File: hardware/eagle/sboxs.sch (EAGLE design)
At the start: 32 parts, among them U1 TXS0101_DBV_6

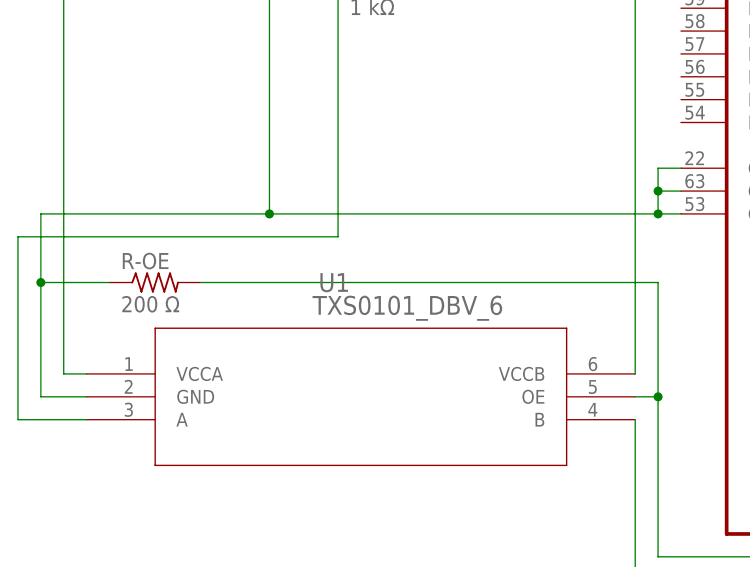
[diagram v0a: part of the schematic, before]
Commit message: update to small pcb v0.2 and minor changes to overall schematic
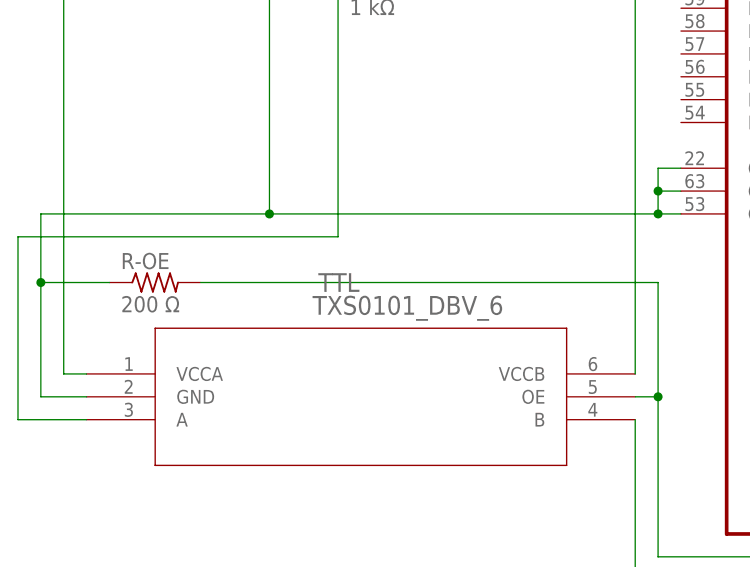
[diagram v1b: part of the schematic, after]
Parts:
- renumbered U1 to TTL
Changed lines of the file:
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@@
 <part name="LGC" library="solpad" library_urn="urn:adsk.eagle:library:364" deviceset="LSP10" device="" package3d_urn="urn:adsk.eagle:package:26501/1"/>
 <part name="BTN-GND" library="wirepad" library_urn="urn:adsk.eagle:library:412" deviceset="1,6/0,8" device="" package3d_urn="urn:adsk.eagle:package:30830/1"/>
-<part name="U1" library="txs0101" deviceset="TXS0101_DBV_6" device=""/>
+<part name="TTL" library="txs0101" deviceset="TXS0101_DBV_6" device=""/>
 <part name="R-OE" library="resistor" library_urn="urn:adsk.eagle:library:348" deviceset="R-US_" device="0207/12" package3d_urn="urn:adsk.eagle:package:25938/1" value="200 Ω"/>
 <part name="R-DATA" library="resistor" library_urn="urn:adsk.eagle:library:348" deviceset="R-US_" device="0207/12" package3d_urn="urn:adsk.eagle:package:25938/1" value="1 kΩ"/>
@@
 <instance part="LGC" gate="1" x="20.32" y="104.14"/>
 <instance part="BTN-GND" gate="P" x="55.88" y="154.94" rot="R270"/>
-<instance part="U1" gate="A" x="-15.24" y="35.56"/>
+<instance part="TTL" gate="A" x="-15.24" y="35.56"/>
 <instance part="R-OE" gate="G$1" x="-7.62" y="45.72"/>
 <instance part="R-DATA" gate="G$1" x="17.78" y="78.74"/>
@@
 <wire x1="12.7" y1="78.74" x2="12.7" y2="50.8" width="0.1524" layer="91"/>
 <wire x1="12.7" y1="50.8" x2="-22.86" y2="50.8" width="0.1524" layer="91"/>
-<pinref part="U1" gate="A" pin="A"/>
+<pinref part="TTL" gate="A" pin="A"/>
 <wire x1="-22.86" y1="50.8" x2="-22.86" y2="30.48" width="0.1524" layer="91"/>
 <wire x1="-22.86" y1="30.48" x2="-15.24" y2="30.48" width="0.1524" layer="91"/>
@@
 <net name="N$29" class="0">
 <segment>
-<pinref part="U1" gate="A" pin="B"/>
+<pinref part="TTL" gate="A" pin="B"/>
 <wire x1="45.72" y1="30.48" x2="45.72" y2="12.7" width="0.1524" layer="91"/>
 <wire x1="45.72" y1="12.7" x2="142.24" y2="12.7" width="0.1524" layer="91"/>
@@
 <net name="N$30" class="0">
 <segment>
-<pinref part="U1" gate="A" pin="OE"/>
+<pinref part="TTL" gate="A" pin="OE"/>
 <wire x1="45.72" y1="33.02" x2="48.26" y2="33.02" width="0.1524" layer="91"/>
 <wire x1="48.26" y1="33.02" x2="48.26" y2="45.72" width="0.1524" layer="91"/>
@@
 <pinref part="BTN-GND" gate="P" pin="P"/>
 <wire x1="55.88" y1="152.4" x2="55.88" y2="139.7" width="0.1524" layer="91"/>
-<pinref part="U1" gate="A" pin="GND"/>
+<pinref part="TTL" gate="A" pin="GND"/>
 <wire x1="-15.24" y1="33.02" x2="-20.32" y2="33.02" width="0.1524" layer="91"/>
 <wire x1="-20.32" y1="33.02" x2="-20.32" y2="45.72" width="0.1524" layer="91"/>
@@
 <junction x="48.26" y="127"/>
 <junction x="48.26" y="124.46"/>
-<pinref part="U1" gate="A" pin="VCCB"/>
+<pinref part="TTL" gate="A" pin="VCCB"/>
 <wire x1="45.72" y1="35.56" x2="45.72" y2="109.22" width="0.1524" layer="91"/>
 <wire x1="45.72" y1="109.22" x2="43.18" y2="109.22" width="0.1524" layer="91"/>
@@
 <wire x1="20.32" y1="99.06" x2="20.32" y2="88.9" width="0.1524" layer="91"/>
 <wire x1="20.32" y1="88.9" x2="-17.78" y2="88.9" width="0.1524" layer="91"/>
-<pinref part="U1" gate="A" pin="VCCA"/>
+<pinref part="TTL" gate="A" pin="VCCA"/>
 <wire x1="-17.78" y1="88.9" x2="-17.78" y2="35.56" width="0.1524" layer="91"/>
 <wire x1="-17.78" y1="35.56" x2="-15.24" y2="35.56" width="0.1524" layer="91"/>
